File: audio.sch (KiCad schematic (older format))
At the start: 23 parts

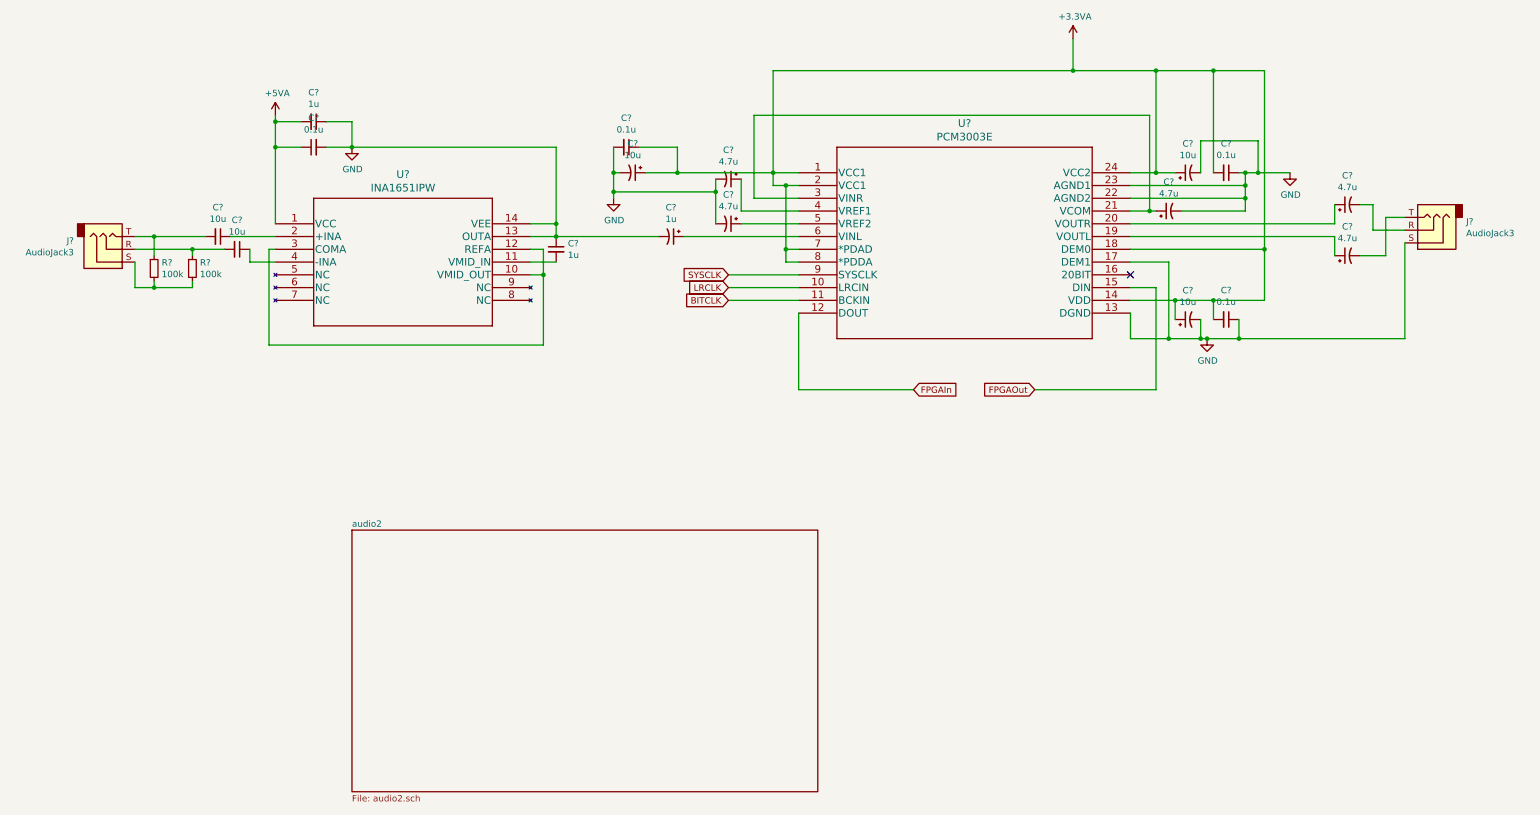
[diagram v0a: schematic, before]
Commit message: Connect DAC/ADC to FPGA
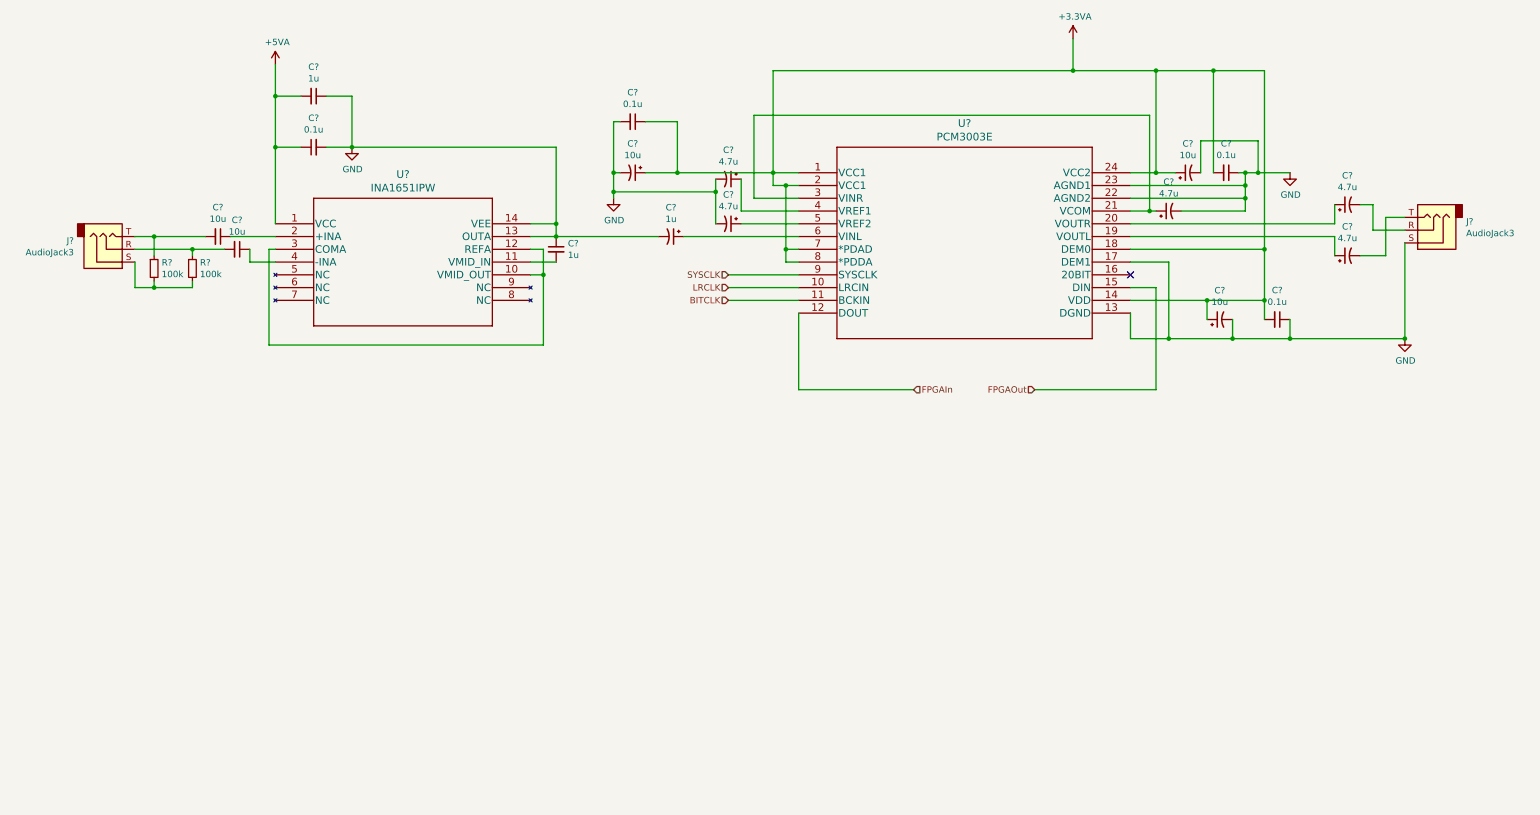
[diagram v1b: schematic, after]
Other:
- moved on the sheet: C?
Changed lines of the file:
@@
 $Descr A3 16535 11693
 encoding utf-8
-Sheet 5 8
+Sheet 3 5
 Title ""
 Date ""
@@
 Wire Wire Line
 	8500 3700 8050 3700
-Text GLabel 9400 5000 2    50   Input ~ 0
-FPGAIn
 Wire Wire Line
 	11100 4200 11300 4200
@@
 	12150 3900 12150 4300
 Wire Wire Line
-	11700 4600 11950 4600
-Connection ~ 11700 4600
-Wire Wire Line
-	11400 4600 11650 4600
-Wire Wire Line
 	11400 4000 11400 4600
 $Comp
 L power:GND #PWR0144
 U 1 1 5D923A6D
-P 11700 4600
-F 0 "#PWR0144" H 11700 4350 50  0001 C CNN
-F 1 "GND" H 11705 4427 50  0000 C CNN
-F 2 "" H 11700 4600 50  0001 C CNN
-F 3 "" H 11700 4600 50  0001 C CNN
-	1    11700 4600
+P 13250 4600
+F 0 "#PWR0144" H 13250 4350 50  0001 C CNN
+F 1 "GND" H 13255 4427 50  0000 C CNN
+F 2 "" H 13250 4600 50  0001 C CNN
+F 3 "" H 13250 4600 50  0001 C CNN
+	1    13250 4600
 	1    0    0    -1
 $EndComp
@@
 L Device:C_Small C?
 U 1 1 5DA0CB9C
-P 11850 4450
-F 0 "C?" V 11621 4450 50  0000 C CNN
-F 1 "0.1u" V 11712 4450 50  0000 C CNN
-F 2 "" H 11850 4450 50  0001 C CNN
-F 3 "~" H 11850 4450 50  0001 C CNN
-	1    11850 4450
-	0    1    1    0
-$EndComp
-$Comp
-L Device:CP1_Small C?
-U 1 1 5DA3F11E
-P 11550 4450
-F 0 "C?" V 11778 4450 50  0000 C CNN
-F 1 "10u" V 11687 4450 50  0000 C CNN
-F 2 "" H 11550 4450 50  0001 C CNN
-F 3 "~" H 11550 4450 50  0001 C CNN
-	1    11550 4450
-	0    -1   -1   0
-$EndComp
-Wire Wire Line
-	11450 4450 11450 4300
-Wire Wire Line
-	11100 4300 11450 4300
-Wire Wire Line
-	11450 4300 11750 4300
-Connection ~ 11450 4300
-Wire Wire Line
-	11950 4450 11950 4600
-Text GLabel 7950 4100 0    50   Input ~ 0
-SYSCLK
-Text GLabel 7950 4200 0    50   Input ~ 0
-LRCLK
-Text GLabel 7950 4300 0    50   Input ~ 0
-BITCLK
+P 12250 4450
+F 0 "C?" V 12021 4450 50  0000 C CNN
+F 1 "0.1u" V 12112 4450 50  0000 C CNN
+F 2 "" H 12250 4450 50  0001 C CNN
+F 3 "~" H 12250 4450 50  0001 C CNN
+	1    12250 4450
+	0    1    1    0
+$EndComp
+Wire Wire Line
+	11700 4450 11700 4300
+Wire Wire Line
+	12350 4450 12350 4600
 Wire Wire Line
 	7950 4200 8500 4200
@@
 Wire Wire Line
 	11300 2500 11750 2500
-Text GLabel 10350 5000 0    50   Input ~ 0
-FPGAOut
 Wire Wire Line
 	11300 5000 10350 5000
-$Sheet
-S 5000 6100 3650 2050
-U 5DA2387E
-F0 "audio2" 50
-F1 "audio2.sch" 50
-$EndSheet
 $Comp
 L Device:R_Small R?
@@
 L power:+5VA #PWR?
 U 1 1 5DB17568
-P 4400 2850
-F 0 "#PWR?" H 4400 2700 50  0001 C CNN
-F 1 "+5VA" H 4415 3023 50  0000 C CNN
-F 2 "" H 4400 2850 50  0001 C CNN
-F 3 "" H 4400 2850 50  0001 C CNN
-	1    4400 2850
+P 4400 2450
+F 0 "#PWR?" H 4400 2300 50  0001 C CNN
+F 1 "+5VA" H 4415 2623 50  0000 C CNN
+F 2 "" H 4400 2450 50  0001 C CNN
+F 3 "" H 4400 2450 50  0001 C CNN
+	1    4400 2450
 	1    0    0    -1
 $EndComp
@@
 $EndComp
 Wire Wire Line
-	5000 3100 5000 2900
-Wire Wire Line
-	5000 2900 4800 2900
-Connection ~ 4400 2900
-Wire Wire Line
-	4400 2900 4400 2850
+	5000 3100 5000 2700
+Wire Wire Line
+	5000 2700 4800 2700
+Connection ~ 4400 2700
+Wire Wire Line
+	4400 2700 4400 2450
 Wire Wire Line
 	5000 3100 4800 3100
@@
 Connection ~ 4400 3100
 Wire Wire Line
-	4400 3100 4400 2900
+	4400 3100 4400 2700
 $Comp
 L Device:C_Small C?
 U 1 1 5DB42CDB
-P 4700 2900
-F 0 "C?" V 4471 2900 50  0000 C CNN
-F 1 "1u" V 4562 2900 50  0000 C CNN
-F 2 "" H 4700 2900 50  0001 C CNN
-F 3 "~" H 4700 2900 50  0001 C CNN
-	1    4700 2900
-	0    1    1    0
-$EndComp
-Wire Wire Line
-	4600 2900 4400 2900
+P 4700 2700
+F 0 "C?" V 4471 2700 50  0000 C CNN
+F 1 "1u" V 4562 2700 50  0000 C CNN
+F 2 "" H 4700 2700 50  0001 C CNN
+F 3 "~" H 4700 2700 50  0001 C CNN
+	1    4700 2700
+	0    1    1    0
+$EndComp
+Wire Wire Line
+	4600 2700 4400 2700
 $Comp
 L Device:C_Small C?
@@
 	13250 3850 13250 4600
 Wire Wire Line
-	13250 4600 11950 4600
-Connection ~ 11950 4600
+	13250 4600 12350 4600
 $Comp
 L Connector:AudioJack3 J?
@@
 NoConn ~ 11100 4100
 Wire Wire Line
-	11650 4450 11650 4600
-Connection ~ 11650 4600
-Wire Wire Line
-	11650 4600 11700 4600
-Wire Wire Line
-	11750 4450 11750 4300
-Connection ~ 11750 4300
-Wire Wire Line
-	11750 4300 12150 4300
+	11900 4450 11900 4600
+Wire Wire Line
+	12150 4450 12150 4300
 Wire Wire Line
 	11650 3300 11650 3050
@@
 Wire Wire Line
 	7100 3300 7050 3300
+Wire Wire Line
+	7050 3300 7050 3450
+Wire Wire Line
+	7550 2900 7550 3300
+Connection ~ 7550 3300
+Wire Wire Line
+	7550 3300 8300 3300
+Wire Wire Line
+	7300 2900 7550 2900
+$Comp
+L Device:C_Small C?
+U 1 1 5D8A5F6F
+P 7200 2900
+F 0 "C?" V 6971 2900 50  0000 C CNN
+F 1 "0.1u" V 7062 2900 50  0000 C CNN
+F 2 "" H 7200 2900 50  0001 C CNN
+F 3 "~" H 7200 2900 50  0001 C CNN
+	1    7200 2900
+	0    1    1    0
+$EndComp
+Wire Wire Line
+	6600 3800 7400 3800
+Wire Wire Line
+	7050 3300 7050 2900
+Wire Wire Line
+	7050 2900 7100 2900
 Connection ~ 7050 3300
-Wire Wire Line
-	7050 3300 7050 3450
-Wire Wire Line
-	7550 3100 7550 3300
-Connection ~ 7550 3300
-Wire Wire Line
-	7550 3300 8300 3300
-Wire Wire Line
-	7050 3100 7050 3300
-Wire Wire Line
-	7250 3100 7550 3100
-$Comp
-L Device:C_Small C?
-U 1 1 5D8A5F6F
-P 7150 3100
-F 0 "C?" V 6921 3100 50  0000 C CNN
-F 1 "0.1u" V 7012 3100 50  0000 C CNN
-F 2 "" H 7150 3100 50  0001 C CNN
-F 3 "~" H 7150 3100 50  0001 C CNN
-	1    7150 3100
-	0    1    1    0
-$EndComp
-Wire Wire Line
-	6600 3800 7400 3800
+Connection ~ 13250 4600
+Connection ~ 12150 4300
+Connection ~ 12350 4600
+Connection ~ 11700 4300
+Wire Wire Line
+	11700 4300 12150 4300
+Connection ~ 11900 4600
+Wire Wire Line
+	11900 4600 12350 4600
+Wire Wire Line
+	11400 4600 11900 4600
+Wire Wire Line
+	11100 4300 11700 4300
+$Comp
+L Device:CP1_Small C?
+U 1 1 5DA3F11E
+P 11800 4450
+F 0 "C?" V 12028 4450 50  0000 C CNN
+F 1 "10u" V 11937 4450 50  0000 C CNN
+F 2 "" H 11800 4450 50  0001 C CNN
+F 3 "~" H 11800 4450 50  0001 C CNN
+	1    11800 4450
+	0    -1   -1   0
+$EndComp
+Text HLabel 7950 4100 0    50   Input ~ 0
+SYSCLK
+Text HLabel 7950 4200 0    50   Input ~ 0
+LRCLK
+Text HLabel 7950 4300 0    50   Input ~ 0
+BITCLK
+Text HLabel 9400 5000 2    50   Input ~ 0
+FPGAIn
+Text HLabel 10350 5000 0    50   Input ~ 0
+FPGAOut
 $EndSCHEMATC

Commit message: Add audio jack footprint
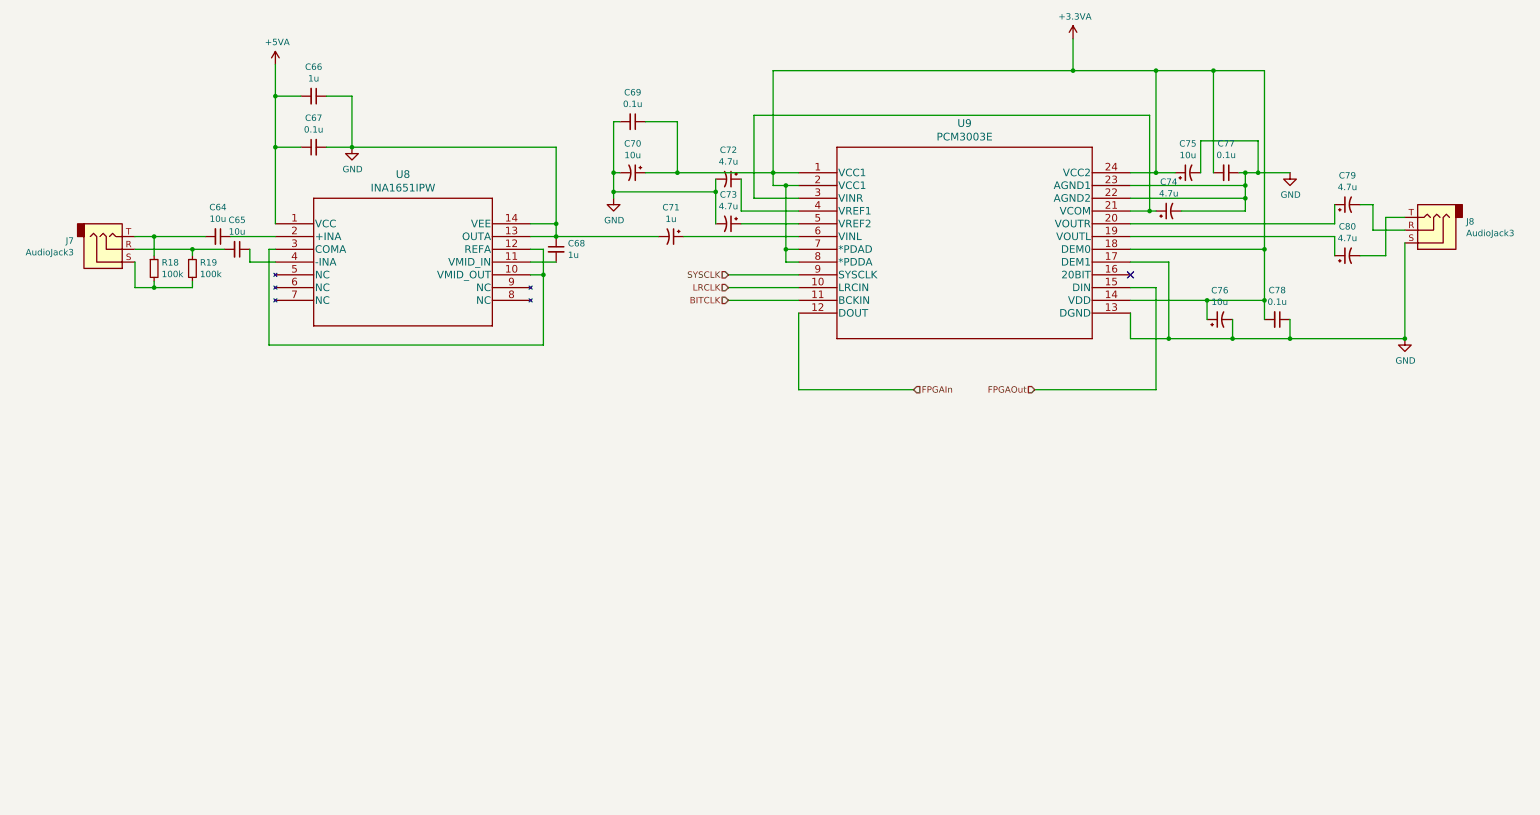
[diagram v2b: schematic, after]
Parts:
- J7, J8: renamed from J?; footprint (none) -> Connector_Audio:Jack_3.5mm_CUI_SJ-3523-SMT_Horizontal
- gave numbers to parts that had none: 21
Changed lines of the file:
@@
 $EndDescr
 $Comp
-L pcm3003:PCM3003E U?
+L pcm3003:PCM3003E U9
 U 1 1 5D8E191D
 P 8500 3300
-F 0 "U?" H 9800 3687 60  0000 C CNN
+F 0 "U9" H 9800 3687 60  0000 C CNN
 F 1 "PCM3003E" H 9800 3581 60  0000 C CNN
 F 2 "DB24" H 9800 3540 60  0001 C CNN
@@
 	7600 3800 8500 3800
 $Comp
-L Device:CP1_Small C?
+L Device:CP1_Small C71
 U 1 1 5D8B87E0
 P 7500 3800
-F 0 "C?" V 7272 3800 50  0000 C CNN
+F 0 "C71" V 7272 3800 50  0000 C CNN
 F 1 "1u" V 7363 3800 50  0000 C CNN
 F 2 "" H 7500 3800 50  0001 C CNN
@@
 $EndComp
 $Comp
-L Device:CP1_Small C?
+L Device:CP1_Small C72
 U 1 1 5D928F6A
 P 7950 3350
-F 0 "C?" V 7722 3350 50  0000 C CNN
+F 0 "C72" V 7722 3350 50  0000 C CNN
 F 1 "4.7u" V 7813 3350 50  0000 C CNN
 F 2 "" H 7950 3350 50  0001 C CNN
@@
 $EndComp
 $Comp
-L Device:CP1_Small C?
+L Device:CP1_Small C73
 U 1 1 5D944B3F
 P 7950 3700
-F 0 "C?" V 7722 3700 50  0000 C CNN
+F 0 "C73" V 7722 3700 50  0000 C CNN
 F 1 "4.7u" V 7813 3700 50  0000 C CNN
 F 2 "" H 7950 3700 50  0001 C CNN
@@
 	11300 4200 11300 5000
 $Comp
-L Device:C_Small C?
+L Device:C_Small C77
 U 1 1 5DA48199
 P 11850 3300
-F 0 "C?" V 11621 3300 50  0000 C CNN
+F 0 "C77" V 11621 3300 50  0000 C CNN
 F 1 "0.1u" V 11712 3300 50  0000 C CNN
 F 2 "" H 11850 3300 50  0001 C CNN
@@
 $EndComp
 $Comp
-L Device:CP1_Small C?
+L Device:CP1_Small C75
 U 1 1 5DA4819F
 P 11550 3300
-F 0 "C?" V 11778 3300 50  0000 C CNN
+F 0 "C75" V 11778 3300 50  0000 C CNN
 F 1 "10u" V 11687 3300 50  0000 C CNN
 F 2 "" H 11550 3300 50  0001 C CNN
@@
 $EndComp
 $Comp
-L Device:CP1_Small C?
+L Device:CP1_Small C74
 U 1 1 5DA4E4FB
 P 11400 3600
-F 0 "C?" V 11628 3600 50  0000 C CNN
+F 0 "C74" V 11628 3600 50  0000 C CNN
 F 1 "4.7u" V 11537 3600 50  0000 C CNN
 F 2 "" H 11400 3600 50  0001 C CNN
@@
 	7300 3300 7550 3300
 $Comp
-L Device:CP1_Small C?
+L Device:CP1_Small C70
 U 1 1 5D8A6788
 P 7200 3300
-F 0 "C?" V 6972 3300 50  0000 C CNN
+F 0 "C70" V 6972 3300 50  0000 C CNN
 F 1 "10u" V 7063 3300 50  0000 C CNN
 F 2 "" H 7200 3300 50  0001 C CNN
@@
 Connection ~ 11400 4600
 $Comp
-L ina1651:INA1651IPW U?
+L ina1651:INA1651IPW U8
 U 1 1 5DAB3F99
 P 4400 3700
-F 0 "U?" H 5400 4087 60  0000 C CNN
+F 0 "U8" H 5400 4087 60  0000 C CNN
 F 1 "INA1651IPW" H 5400 3981 60  0000 C CNN
 F 2 "PW0014A_N" H 5400 3940 60  0001 C CNN
@@
 $EndComp
 $Comp
-L Device:C_Small C?
+L Device:C_Small C78
 U 1 1 5DA0CB9C
 P 12250 4450
-F 0 "C?" V 12021 4450 50  0000 C CNN
+F 0 "C78" V 12021 4450 50  0000 C CNN
 F 1 "0.1u" V 12112 4450 50  0000 C CNN
 F 2 "" H 12250 4450 50  0001 C CNN
@@
 	8500 4300 7950 4300
 $Comp
-L Device:CP1_Small C?
+L Device:CP1_Small C79
 U 1 1 5D8E8914
 P 12800 3550
-F 0 "C?" V 13028 3550 50  0000 C CNN
+F 0 "C79" V 13028 3550 50  0000 C CNN
 F 1 "4.7u" V 12937 3550 50  0000 C CNN
 F 2 "" H 12800 3550 50  0001 C CNN
@@
 $EndComp
 $Comp
-L Device:CP1_Small C?
+L Device:CP1_Small C80
 U 1 1 5D8EDDDB
 P 12800 3950
-F 0 "C?" V 13028 3950 50  0000 C CNN
+F 0 "C80" V 13028 3950 50  0000 C CNN
 F 1 "4.7u" V 12937 3950 50  0000 C CNN
 F 2 "" H 12800 3950 50  0001 C CNN
@@
 	11300 5000 10350 5000
 $Comp
-L Device:R_Small R?
+L Device:R_Small R18
 U 1 1 5DAE583D
 P 3450 4050
-F 0 "R?" H 3509 4096 50  0000 L CNN
+F 0 "R18" H 3509 4096 50  0000 L CNN
 F 1 "100k" H 3509 4005 50  0000 L CNN
 F 2 "" H 3450 4050 50  0001 C CNN
@@
 $EndComp
 $Comp
-L Device:R_Small R?
+L Device:R_Small R19
 U 1 1 5DAE6F3E
 P 3750 4050
-F 0 "R?" H 3809 4096 50  0000 L CNN
+F 0 "R19" H 3809 4096 50  0000 L CNN
 F 1 "100k" H 3809 4005 50  0000 L CNN
 F 2 "" H 3750 4050 50  0001 C CNN
@@
 	3450 4200 3750 4200
 $Comp
-L Device:C_Small C?
+L Device:C_Small C64
 U 1 1 5DAECECC
 P 3950 3800
-F 0 "C?" V 3721 3800 50  0000 C CNN
+F 0 "C64" V 3721 3800 50  0000 C CNN
 F 1 "10u" V 3812 3800 50  0000 C CNN
 F 2 "" H 3950 3800 50  0001 C CNN
@@
 $EndComp
 $Comp
-L Device:C_Small C?
+L Device:C_Small C65
 U 1 1 5DAED70A
 P 4100 3900
-F 0 "C?" V 3871 3900 50  0000 C CNN
+F 0 "C65" V 3871 3900 50  0000 C CNN
 F 1 "10u" V 3962 3900 50  0000 C CNN
 F 2 "" H 4100 3900 50  0001 C CNN
@@
 	3450 3800 3850 3800
 $Comp
-L power:+5VA #PWR?
+L power:+5VA #PWR0164
 U 1 1 5DB17568
 P 4400 2450
-F 0 "#PWR?" H 4400 2300 50  0001 C CNN
+F 0 "#PWR0164" H 4400 2300 50  0001 C CNN
 F 1 "+5VA" H 4415 2623 50  0000 C CNN
 F 2 "" H 4400 2450 50  0001 C CNN
@@
 	6400 4000 6600 4000
 $Comp
-L Device:C_Small C?
+L Device:C_Small C68
 U 1 1 5DB1DC64
 P 6600 3900
-F 0 "C?" H 6692 3946 50  0000 L CNN
+F 0 "C68" H 6692 3946 50  0000 L CNN
 F 1 "1u" H 6692 3855 50  0000 L CNN
 F 2 "" H 6600 3900 50  0001 C CNN
@@
 	4400 3700 4400 3100
 $Comp
-L power:GND #PWR?
+L power:GND #PWR0165
 U 1 1 5DB39F15
 P 5000 3100
-F 0 "#PWR?" H 5000 2850 50  0001 C CNN
+F 0 "#PWR0165" H 5000 2850 50  0001 C CNN
 F 1 "GND" H 5005 2927 50  0000 C CNN
 F 2 "" H 5000 3100 50  0001 C CNN
@@
 	4400 3100 4400 2700
 $Comp
-L Device:C_Small C?
+L Device:C_Small C66
 U 1 1 5DB42CDB
 P 4700 2700
-F 0 "C?" V 4471 2700 50  0000 C CNN
+F 0 "C66" V 4471 2700 50  0000 C CNN
 F 1 "1u" V 4562 2700 50  0000 C CNN
 F 2 "" H 4700 2700 50  0001 C CNN
@@
 	4600 2700 4400 2700
 $Comp
-L Device:C_Small C?
+L Device:C_Small C67
 U 1 1 5DB4CAEF
 P 4700 3100
-F 0 "C?" V 4929 3100 50  0000 C CNN
+F 0 "C67" V 4929 3100 50  0000 C CNN
 F 1 "0.1u" V 4838 3100 50  0000 C CNN
 F 2 "" H 4700 3100 50  0001 C CNN
@@
 Connection ~ 6600 3800
 $Comp
-L Connector:AudioJack3 J?
+L Connector:AudioJack3 J8
 U 1 1 5D92FF52
 P 13450 3750
-F 0 "J?" H 13170 3683 50  0000 R CNN
+F 0 "J8" H 13170 3683 50  0000 R CNN
 F 1 "AudioJack3" H 13170 3774 50  0000 R CNN
-F 2 "" H 13450 3750 50  0001 C CNN
+F 2 "Connector_Audio:Jack_3.5mm_CUI_SJ-3523-SMT_Horizontal" H 13450 3750 50  0001 C CNN
 F 3 "~" H 13450 3750 50  0001 C CNN
 	1    13450 3750
@@
 	13250 4600 12350 4600
 $Comp
-L Connector:AudioJack3 J?
+L Connector:AudioJack3 J7
 U 1 1 5D973AB4
 P 3100 3900
-F 0 "J?" H 2821 3833 50  0000 R CNN
+F 0 "J7" H 2821 3833 50  0000 R CNN
 F 1 "AudioJack3" H 2821 3924 50  0000 R CNN
-F 2 "" H 3100 3900 50  0001 C CNN
+F 2 "Connector_Audio:Jack_3.5mm_CUI_SJ-3523-SMT_Horizontal" H 3100 3900 50  0001 C CNN
 F 3 "~" H 3100 3900 50  0001 C CNN
 	1    3100 3900
@@
 	7300 2900 7550 2900
 $Comp
-L Device:C_Small C?
+L Device:C_Small C69
 U 1 1 5D8A5F6F
 P 7200 2900
-F 0 "C?" V 6971 2900 50  0000 C CNN
+F 0 "C69" V 6971 2900 50  0000 C CNN
 F 1 "0.1u" V 7062 2900 50  0000 C CNN
 F 2 "" H 7200 2900 50  0001 C CNN
@@
 	11100 4300 11700 4300
 $Comp
-L Device:CP1_Small C?
+L Device:CP1_Small C76
 U 1 1 5DA3F11E
 P 11800 4450
-F 0 "C?" V 12028 4450 50  0000 C CNN
+F 0 "C76" V 12028 4450 50  0000 C CNN
 F 1 "10u" V 11937 4450 50  0000 C CNN
 F 2 "" H 11800 4450 50  0001 C CNN
